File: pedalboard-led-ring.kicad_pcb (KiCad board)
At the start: 2 copper layers, 36 x 28 mm, 16 parts, among them J1 Conn_02x03, U1 TLC5973, U2 LT3494AEDDBPBF

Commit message: Fix connector
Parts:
- C2: value 100nF -> 330nF
- C4: value 0.22uF_0603_25V -> 330nF
- U2: footprint Package_DFN_QFN:DFN-8-1EP_2x3mm_P0.5mm_EP0.61x2.2mm -> Library:DFN300X200X80-9N
- moved L1 0.50 mm to (88.2, 67.1)
- moved C3 0.30 mm to (90.0, 71.2)
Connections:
- J1 pad 1: Net-(J1-SDI) -> VDC
- J1 pad 2: VDC -> Net-(J1-SDI)
- J1 pad 3: Net-(J1-VLED) -> GND
- J1 pad 4: GND -> Net-(J1-VLED)
- J1 pad 5: Net-(U1-SDI) -> VCC
- J1 pad 6: VCC -> Net-(U1-SDI)
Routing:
- net Net-(U1-SDI): track 17.8 -> 15.8 mm
- net VCC: track 3.34 -> 5.36 mm

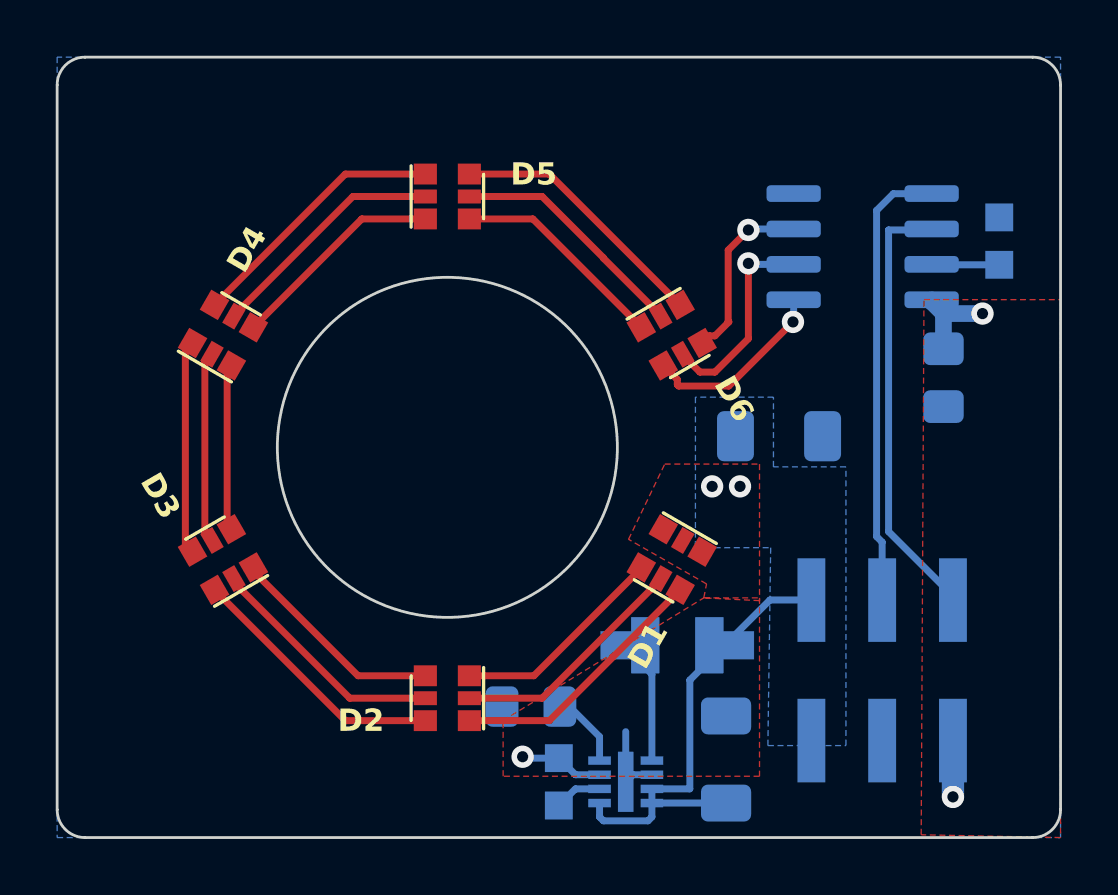
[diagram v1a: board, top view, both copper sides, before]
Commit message: Improve copper ground layers
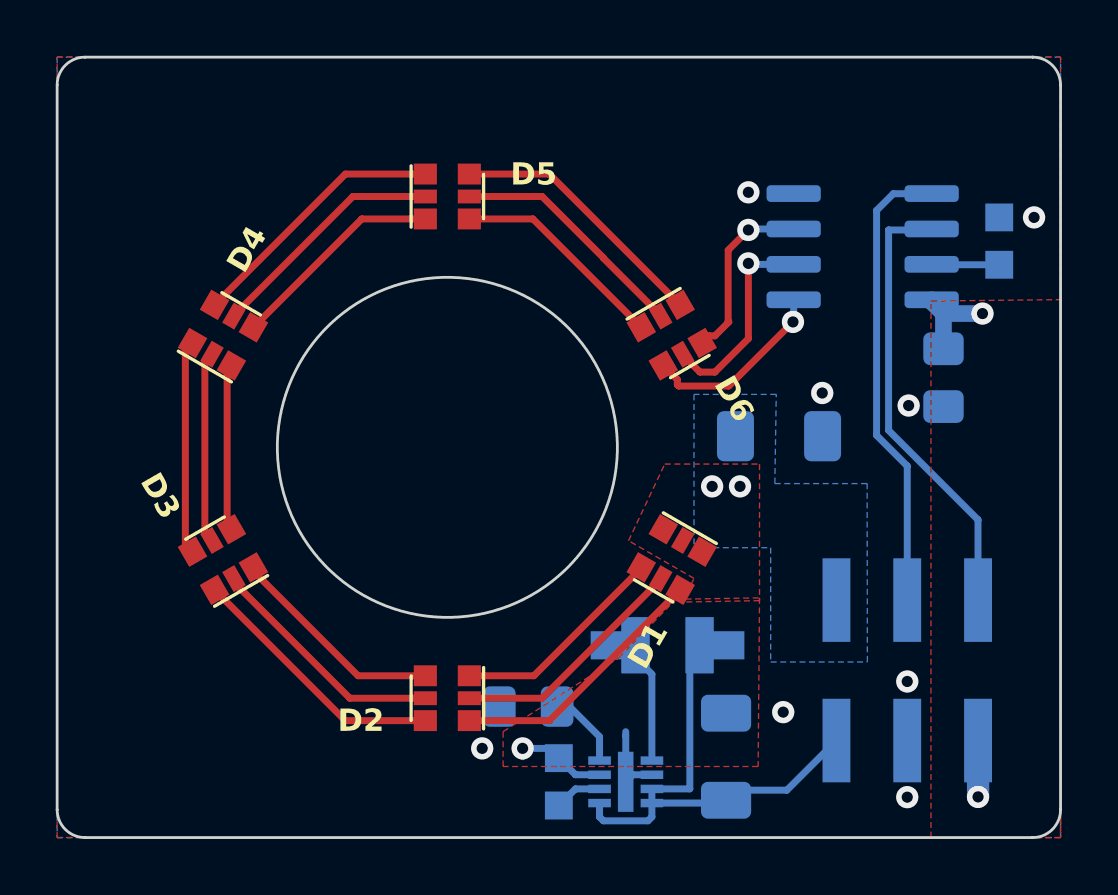
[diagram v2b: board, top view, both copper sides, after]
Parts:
- moved J1 0.90 mm to (96.5, 68.0)
- moved L1 0.35 mm to (87.9, 67.1)
- moved C3 0.10 mm to (90.0, 71.1)
- moved C4 0.10 mm to (82.9, 69.3)
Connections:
- C3 pad 1: Net-(J1-SDI) -> Net-(J1-SDO)
- J1 pad 1: VDC -> Net-(J1-SDO)
- J1 pad 2: Net-(J1-SDI) -> VDC
- L1 pad 2: Net-(J1-SDI) -> Net-(J1-SDO)
- U2 pad 3: Net-(J1-SDI) -> Net-(J1-SDO)
- U2 pad 4: Net-(J1-SDI) -> Net-(J1-SDO)
- U2 pad 5: Net-(J1-SDI) -> Net-(J1-SDO)
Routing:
- net Net-(J1-SDO): track 0.00 -> 17.3 mm
- net Net-(J1-SDI): track 16.5 -> 0.00 mm
- net GND: vias 0 -> 8
- added copper zone on F.Cu, net GND

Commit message: Improve copper ground layers
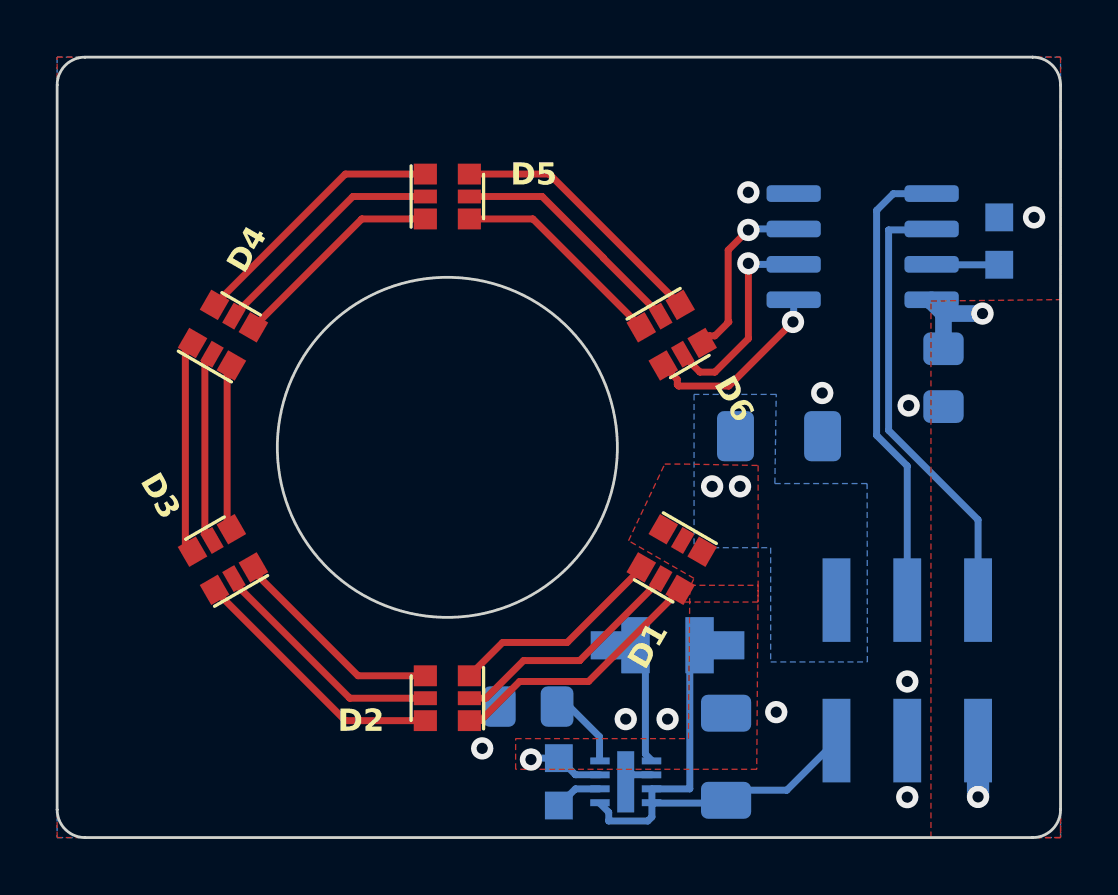
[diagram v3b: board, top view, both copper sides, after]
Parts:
- U2: footprint Library:DFN300X200X80-9N -> Package_DFN_QFN:DFN-8-1EP_2x3mm_P0.5mm_EP0.61x2.2mm
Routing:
- net GND: track 2.85 -> 1.05 mm, vias 8 -> 10
- net VDC: track 3.28 -> 2.73 mm
